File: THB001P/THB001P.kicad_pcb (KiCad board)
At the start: 2 copper layers, 22.9 x 30 mm, 3 parts, among them J1 Conn_01x03, J2 Conn_01x03, U1 THB001P

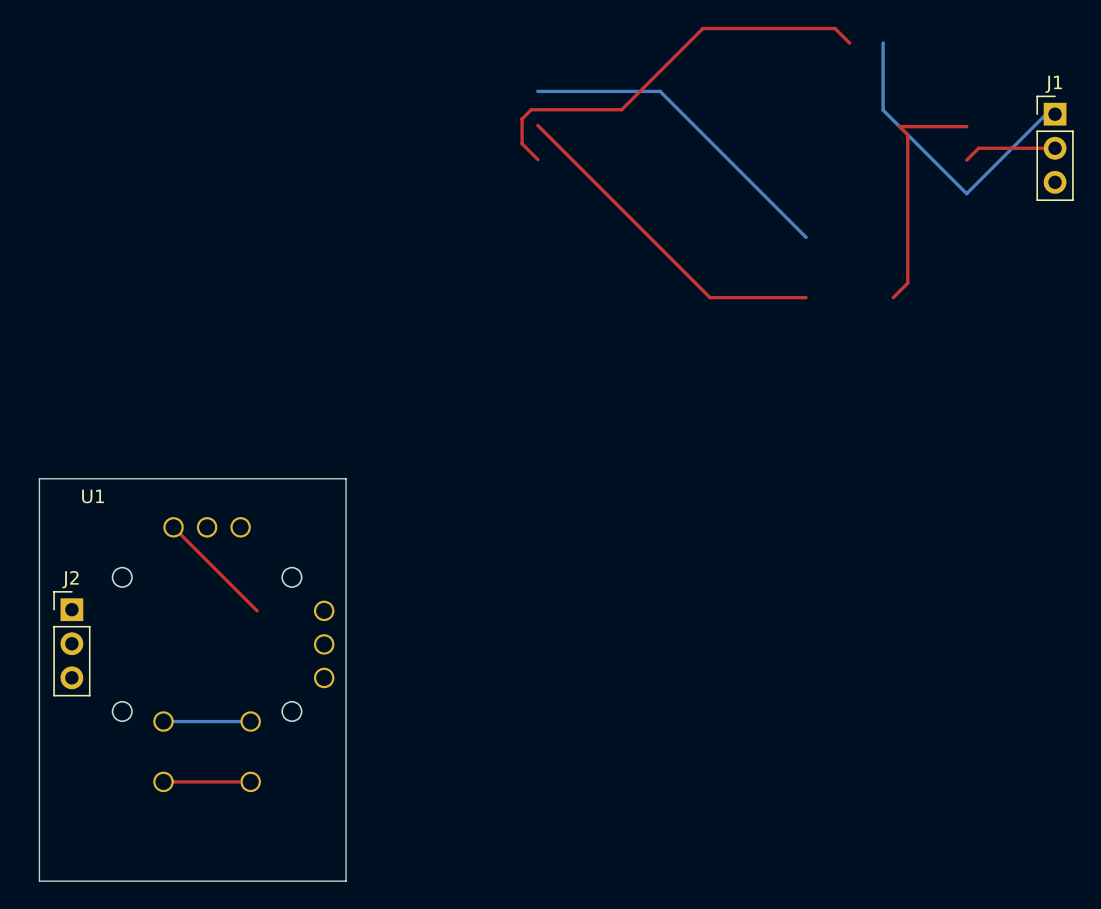
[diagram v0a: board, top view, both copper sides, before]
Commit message: Starting work on Thumbstick (THB001P)
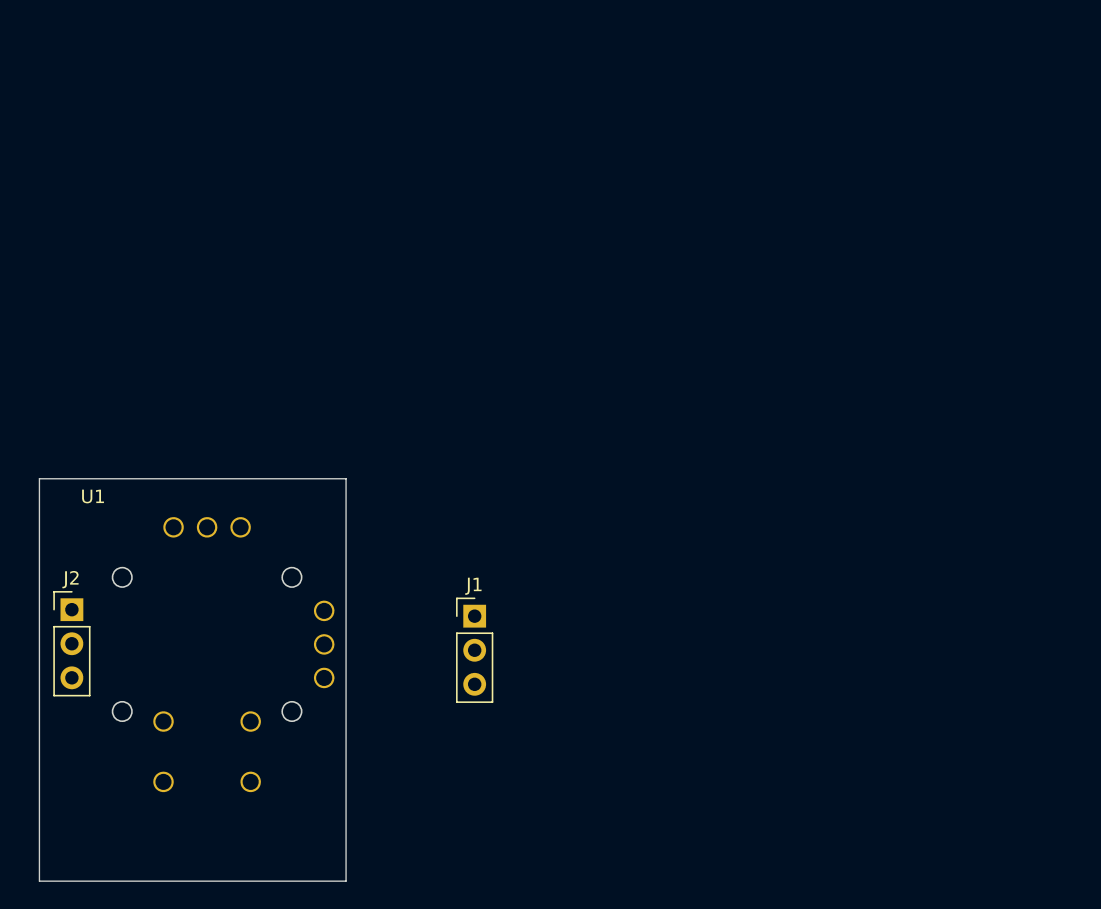
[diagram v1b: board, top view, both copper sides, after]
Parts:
- moved J1 57.2 mm to (132.4, 110.2)
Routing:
- net Net-(J2-Pad2): track 59.1 -> 0.00 mm
- net Net-(J2-Pad3): track 31.2 -> 0.00 mm
- net Net-(J2-Pad1): track 31.0 -> 0.00 mm
- net Net-(J1-Pad1): track 22.9 -> 0.00 mm
- net Net-(J1-Pad2): track 6.95 -> 0.00 mm
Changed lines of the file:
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@@
   )
   (net 0 "")
-  (net 1 "Net-(U1-Pad1)")
-  (net 2 "Net-(U1-Pad2')")
+  (net 1 "Net-(J1-Pad1)")
+  (net 2 "Net-(J1-Pad2)")
   (net 3 "unconnected-(J1-Pad3)")
   (net 4 "Net-(J2-Pad1)")
   (net 5 "Net-(J2-Pad2)")
-  (net 6 "Net-(U1-Pad2)")
+  (net 6 "Net-(J2-Pad3)")
   (footprint "Connector_PinHeader_2.54mm:PinHeader_1x03_P2.54mm_Vertical" (layer "F.Cu")
-    (at 175.72 72.82)
+    (at 132.45 110.245)
     (descr "Through hole straight pin header, 1x03, 2.54mm pitch, single row")
     (tags "Through hole pin header THT 1x03 2.54mm single row")
@@
     (fp_line (start -0.635 -1.27) (end 1.27 -1.27) (layer "F.Fab") (width 0.1))
     (pad "1" thru_hole rect (at 0 0) (size 1.7 1.7) (drill 1) (layers *.Cu *.Mask)
-      (net 1 "Net-(U1-Pad1)") (pinfunction "Pin_1") (pintype "passive"))
+      (net 1 "Net-(J1-Pad1)") (pinfunction "Pin_1") (pintype "passive"))
     (pad "2" thru_hole oval (at 0 2.54) (size 1.7 1.7) (drill 1) (layers *.Cu *.Mask)
-      (net 2 "Net-(U1-Pad2')") (pinfunction "Pin_2") (pintype "passive"))
+      (net 2 "Net-(J1-Pad2)") (pinfunction "Pin_2") (pintype "passive"))
     (pad "3" thru_hole oval (at 0 5.08) (size 1.7 1.7) (drill 1) (layers *.Cu *.Mask)
       (net 3 "unconnected-(J1-Pad3)") (pinfunction "Pin_3") (pintype "passive+no_connect"))
@@
       (net 5 "Net-(J2-Pad2)") (pinfunction "Pin_2") (pintype "passive"))
     (pad "3" thru_hole oval (at 0 5.08) (size 1.7 1.7) (drill 1) (layers *.Cu *.Mask)
-      (net 6 "Net-(U1-Pad2)") (pinfunction "Pin_3") (pintype "passive"))
+      (net 6 "Net-(J2-Pad3)") (pinfunction "Pin_3") (pintype "passive"))
     (model "${KICAD6_3DMODEL_DIR}/Connector_PinHeader_2.54mm.3dshapes/PinHeader_1x03_P2.54mm_Vertical.wrl"
       (offset (xyz 0 0 0))
@@
     (fp_circle (center -6.325 -5) (end -5.6 -5) (layer "Edge.Cuts") (width 0.12) (fill solid))
     (pad "1" thru_hole circle (at 2.5 -8.73) (size 1.524 1.524) (drill 1.2) (layers *.Cu *.Mask)
-      (net 1 "Net-(U1-Pad1)") (pinfunction "1") (pintype "passive"))
+      (net 1 "Net-(J1-Pad1)") (pinfunction "1") (pintype "passive"))
     (pad "1'" thru_hole circle (at 8.73 2.5) (size 1.524 1.524) (drill 1.2) (layers *.Cu *.Mask)
-      (net 1 "Net-(U1-Pad1)") (pinfunction "1'") (pintype "passive"))
+      (net 1 "Net-(J1-Pad1)") (pinfunction "1'") (pintype "passive"))
     (pad "2" thru_hole circle (at 0 -8.73) (size 1.524 1.524) (drill 1.2) (layers *.Cu *.Mask)
-      (net 6 "Net-(U1-Pad2)") (pinfunction "2") (pintype "passive"))
+      (net 6 "Net-(J2-Pad3)") (pinfunction "2") (pintype "passive"))
     (pad "2'" thru_hole circle (at 8.73 0) (size 1.524 1.524) (drill 1.2) (layers *.Cu *.Mask)
-      (net 2 "Net-(U1-Pad2')") (pinfunction "2'") (pintype "passive"))
+      (net 2 "Net-(J1-Pad2)") (pinfunction "2'") (pintype "passive"))
     (pad "3" thru_hole circle (at -2.5 -8.73) (size 1.524 1.524) (drill 1.2) (layers *.Cu *.Mask)
       (net 5 "Net-(J2-Pad2)") (pinfunction "3") (pintype "passive"))
@@
   )
   (gr_rect (start 100 100) (end 122.86 130) (layer "Edge.Cuts") (width 0.1) (fill none))
-  (segment (start 175.72 72.82) (end 175.062 72.82) (width 0.25) (layer "B.Cu") (net 1))
-  (segment (start 162.905 67.517) (end 162.905 72.517) (width 0.25) (layer "B.Cu") (net 1))
-  (segment (start 175.062 72.82) (end 169.135 78.747) (width 0.25) (layer "B.Cu") (net 1))
-  (segment (start 162.905 72.517) (end 169.135 78.747) (width 0.25) (layer "B.Cu") (net 1))
-  (segment (start 175.72 75.36) (end 170.022 75.36) (width 0.25) (layer "F.Cu") (net 2))
-  (segment (start 170.022 75.36) (end 169.135 76.247) (width 0.25) (layer "F.Cu") (net 2))
-  (segment (start 146.278 71.12) (end 137.16 71.12) (width 0.25) (layer "B.Cu") (net 4))
-  (segment (start 115.75 118.1) (end 109.25 118.1) (width 0.25) (layer "B.Cu") (net 4))
-  (segment (start 157.155 81.997) (end 146.278 71.12) (width 0.25) (layer "B.Cu") (net 4))
-  (segment (start 164.741511 85.410489) (end 163.655 86.497) (width 0.25) (layer "F.Cu") (net 5))
-  (segment (start 164.135 73.747) (end 164.741511 74.353511) (width 0.25) (layer "F.Cu") (net 5))
-  (segment (start 115.75 122.6) (end 109.25 122.6) (width 0.25) (layer "F.Cu") (net 5))
-  (segment (start 164.741511 74.353511) (end 164.741511 85.410489) (width 0.25) (layer "F.Cu") (net 5))
-  (segment (start 164.135 73.747) (end 169.135 73.747) (width 0.25) (layer "F.Cu") (net 5))
-  (segment (start 149.997 86.497) (end 157.155 86.497) (width 0.25) (layer "F.Cu") (net 5))
-  (segment (start 137.16 73.66) (end 149.997 86.497) (width 0.25) (layer "F.Cu") (net 5))
-  (segment (start 110 103.62) (end 116.23 109.85) (width 0.25) (layer "F.Cu") (net 5))
-  (segment (start 135.985489 75.025489) (end 137.16 76.2) (width 0.25) (layer "F.Cu") (net 6))
-  (segment (start 149.469511 66.430489) (end 143.414511 72.485489) (width 0.25) (layer "F.Cu") (net 6))
-  (segment (start 136.673501 72.485489) (end 135.985489 73.173501) (width 0.25) (layer "F.Cu") (net 6))
-  (segment (start 143.414511 72.485489) (end 136.673501 72.485489) (width 0.25) (layer "F.Cu") (net 6))
-  (segment (start 159.318489 66.430489) (end 149.469511 66.430489) (width 0.25) (layer "F.Cu") (net 6))
-  (segment (start 160.405 67.517) (end 159.318489 66.430489) (width 0.25) (layer "F.Cu") (net 6))
-  (segment (start 135.985489 73.173501) (end 135.985489 75.025489) (width 0.25) (layer "F.Cu") (net 6))
 )

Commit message: Generating gerbers for board
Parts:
- removed J2: Conn_01x03, Connector_PinHeader_2.54mm:PinHeader_1x03_P2.54mm_Vertical
- J1: value Conn_01x03 -> Conn_01x05; footprint Connector_PinHeader_2.54mm:PinHeader_1x03_P2.54mm_Vertical -> Connector_PinHeader_2.54mm:PinHeader_1x05_P2.54mm_Vertical
- moved J1 25.1 mm to (111.8, 124.5), turned to -90 degrees
- moved U1 4.53 mm to (109.2, 109.2)
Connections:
- J1 pad 1: Net-(J1-Pad1) -> GND
- J1 pad 2: Net-(J1-Pad2) -> +3V3
- J1 pad 3: unconnected-(J1-Pad3) -> /2
- U1 pad 1: Net-(J1-Pad1) -> +3V3
- U1 pad 1': Net-(J1-Pad1) -> +3V3
- U1 pad 2: Net-(J2-Pad3) -> /2
- U1 pad 2': Net-(J1-Pad2) -> /2'
- U1 pad 3: Net-(J2-Pad2) -> GND
- U1 pad 3': Net-(J2-Pad2) -> GND
- U1 pad a: Net-(J2-Pad1) -> /Button
- U1 pad b: Net-(J2-Pad1) -> /Button
- U1 pad c: Net-(J2-Pad2) -> GND
- U1 pad d: Net-(J2-Pad2) -> GND
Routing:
- net /2: track 0.00 -> 34.9 mm
- net +3V3: track 0.00 -> 32.1 mm
- net /2': track 0.00 -> 21.3 mm
- net /Button: track 0.00 -> 17.8 mm
- added copper zone on B.Cu, net GND
- added copper zone on F.Cu, net GND
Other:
- board size 22.9 x 30 mm -> 20.3 x 27.5 mm
- board text added: "3v3"
- board text added: "BTN"
- board text added: "GND"
- board text added: "X"
- board text added: "Y"
